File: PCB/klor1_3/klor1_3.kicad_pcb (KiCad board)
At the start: 2 copper layers, 160 x 118.2 mm, 84 parts, among them J1 MJ-4PP-9, J2 Haptic Buzz, SW1 SW_PUSH-MX_W_LED, SW10 SW_PUSH-MX_W_LED, SW11 SW_PUSH-MX_W_LED, SW12 SW_PUSH-MX_W_LED, SW13 SW_PUSH-MX_W_LED, SW14 SW_PUSH-MX_W_LED, SW15 SW_PUSH-MX_W_LED, SW16 SW_PUSH-MX_W_LED, SW17 SW_PUSH-MX_W_LED, SW18 RotaryEncoder_Switch, SW19 SW_PUSH-MX_W_LED, SW2 SW_PUSH-MX_W_LED, SW20 SW_PUSH-MX_W_LED, SW21 SW_PUSH-MX_W_LED, SW23 5Way-Tactile_K1-1506DN-01, SW3 SW_PUSH-MX_W_LED, SW4 SW_PUSH-MX_W_LED, SW5 SW_PUSH-MX_W_LED, SW6 SW_PUSH-MX_W_LED, SW7 SW_PUSH-MX_W_LED, SW8 SW_PUSH-MX_W_LED, SW9 SW_PUSH-MX_W_LED, U1 ProMicro

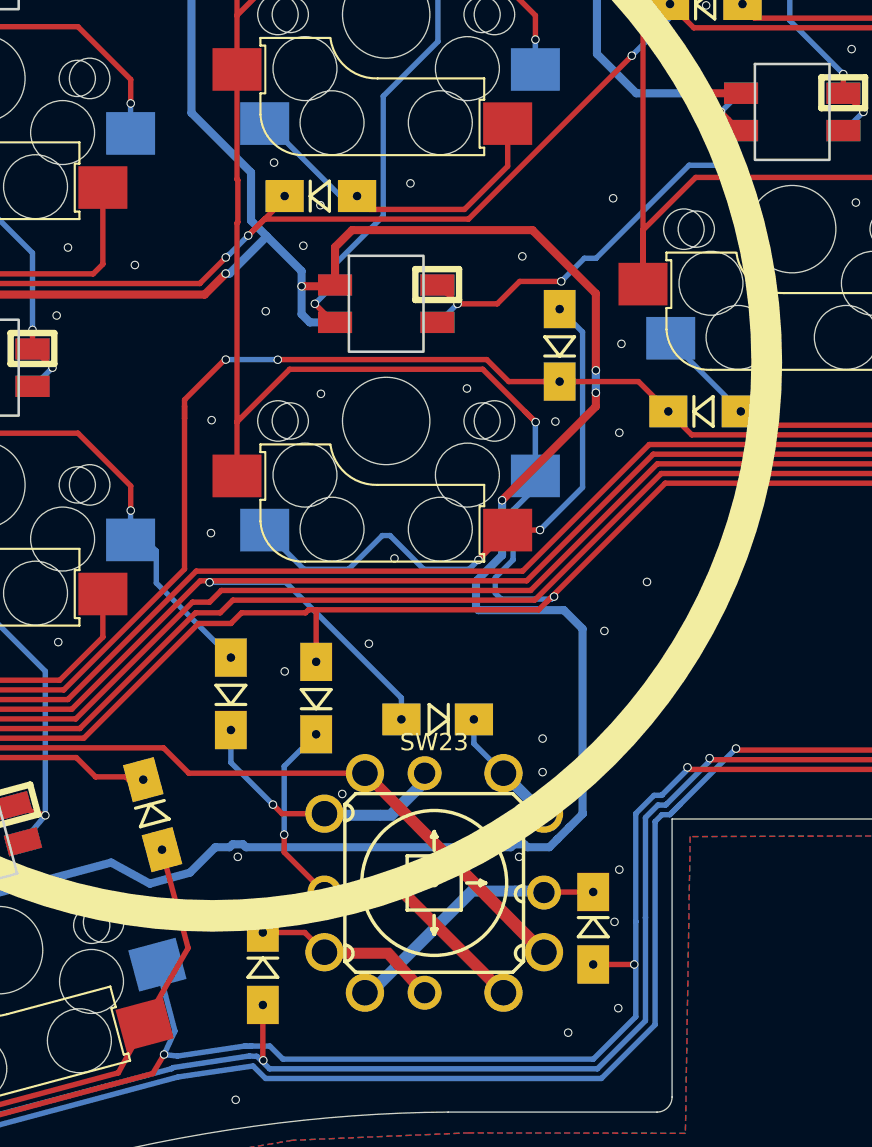
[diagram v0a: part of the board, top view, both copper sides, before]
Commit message: clean up PCB tracks
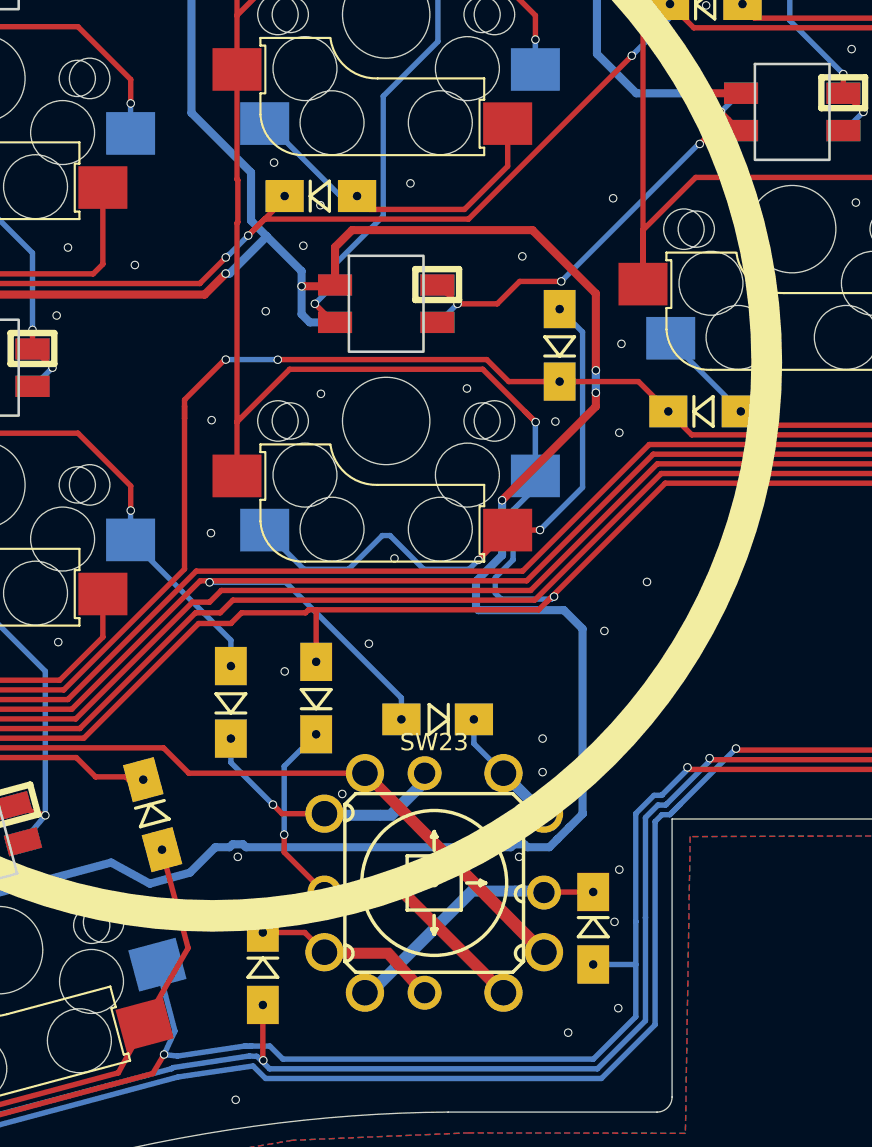
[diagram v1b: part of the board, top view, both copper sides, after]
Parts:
- moved D23 0.40 mm to (132.8, 120.0)
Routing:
- net Net-(SW13B-DOUT): track 22.3 -> 21.6 mm
- net col2: track 332.2 -> 332.3 mm, vias 8 -> 7
